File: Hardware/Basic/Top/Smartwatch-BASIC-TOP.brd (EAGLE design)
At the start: 38 x 38 mm, 60 parts, among them SW6 SWITCH.MOM, SW7 SWITCH.MOM, U2 NRF52832_MODULE_MDBT42, U4 FT231XS

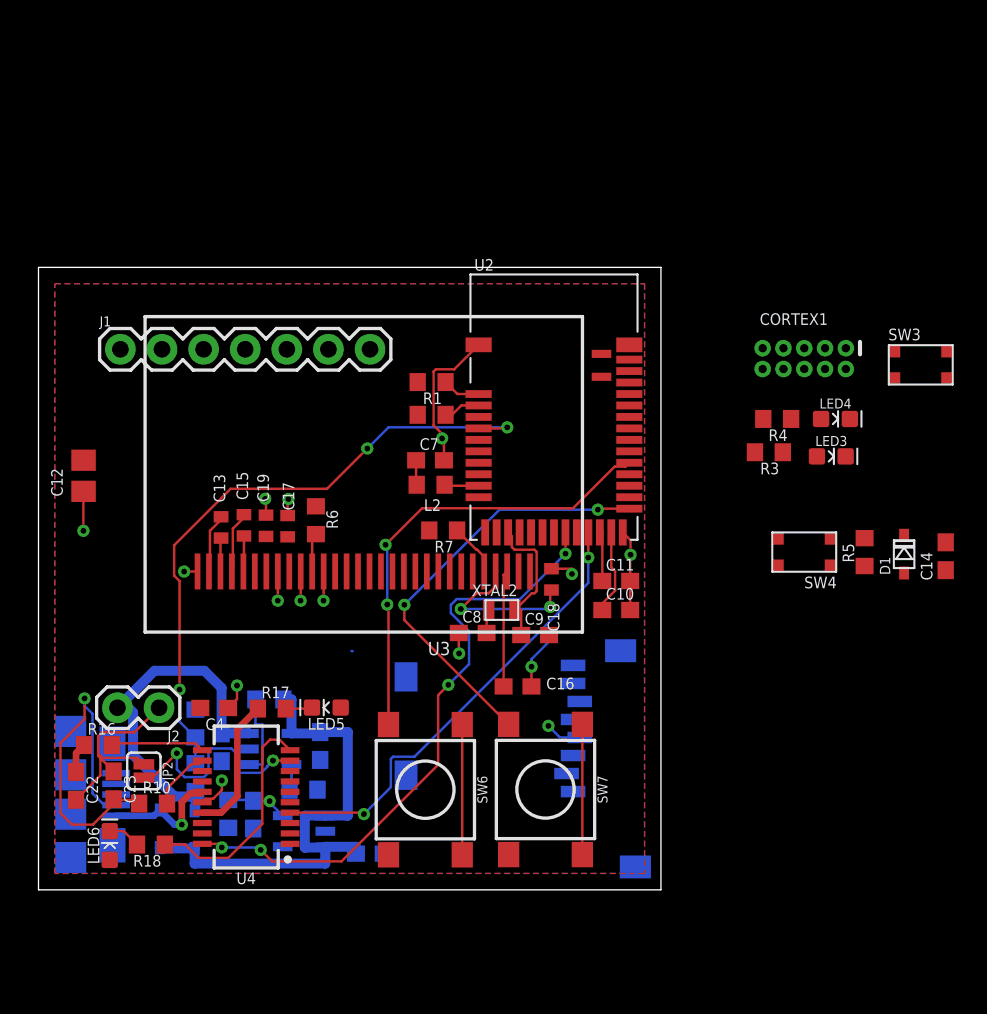
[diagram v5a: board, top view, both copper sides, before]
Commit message: Top board routing started
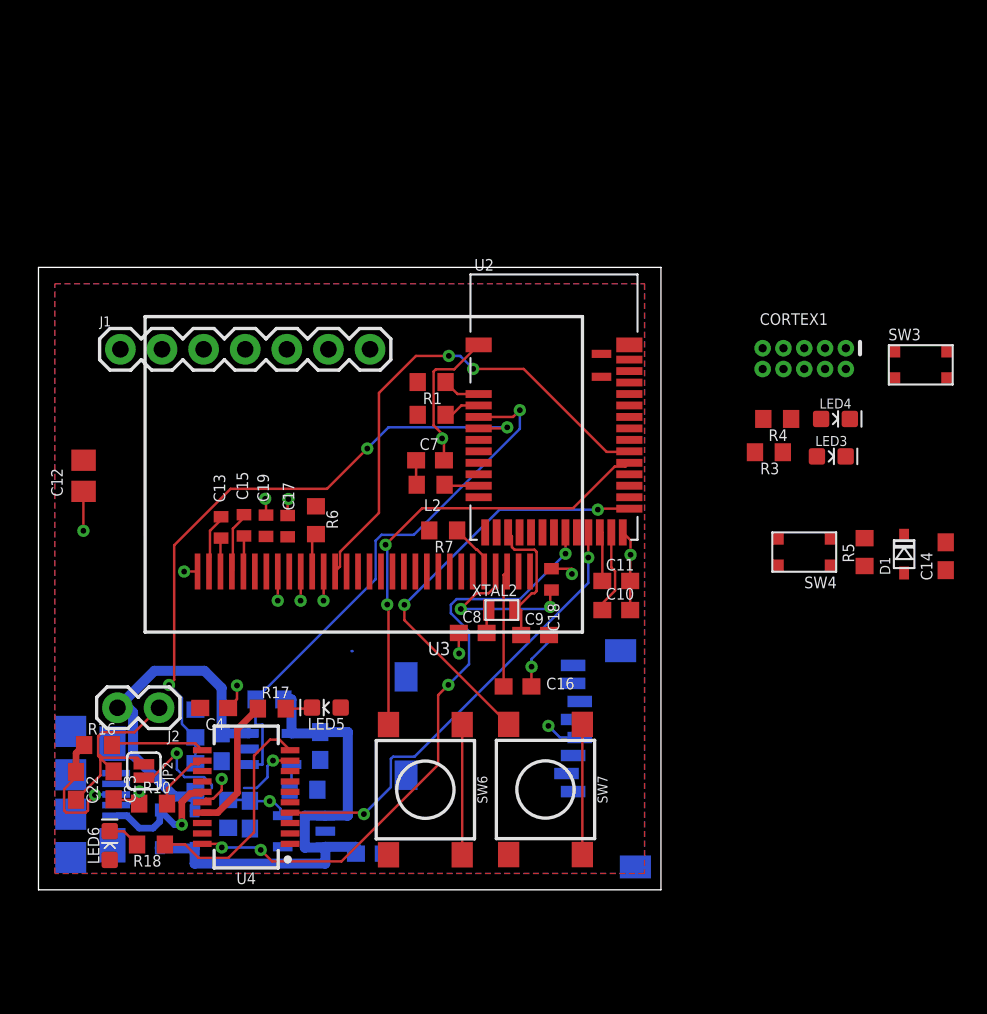
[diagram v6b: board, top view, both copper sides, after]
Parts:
- moved C6 0.20 mm to (12.9, 4.59)
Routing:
- net D16/CS.OLED: track 0.00 -> 30.7 mm, vias 0 -> 2
- net D27/CHRG.STAT: track 5.23 -> 33.4 mm, vias 0 -> 1
- net USB-: track 21.7 -> 4.58 mm
- net USB+: track 1.84 -> 8.48 mm, vias 0 -> 1
- net !CTS: track 14.4 -> 10.8 mm
- net V_USB: track 7.41 -> 8.45 mm

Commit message: Top Board Routed
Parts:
- moved LED6 1.32 mm to (3.51, 1.69), turned to 0 degrees
- moved L2 1.19 mm to (24.8, 25.5), turned to 90 degrees
- moved C7 0.94 mm to (23.3, 25.5), turned to 270 degrees
- moved C16 0.88 mm to (28.6, 13.0), turned to 90 degrees
- moved SD2 0.76 mm to (21.4, 15.4)
- moved R15 0.53 mm to (11.1, 4.62)
- moved C18 0.39 mm to (31.3, 18.6)
- moved C6 0.11 mm to (13.0, 4.60)
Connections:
- net 3.3V: now also J1.4
- net A6/TIA: now also J1.5
- net A7/PPG: now also J1.7
- net D29/LED.CTRL: now also J1.6
- net GND: now also J1.3
- net SCL: now also J1.2
- net SDA: now also J1.1
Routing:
- net SCK: track 0.00 -> 59.4 mm, vias 0 -> 2
- net 3.3V: track 6.14 -> 58.3 mm, vias 2 -> 13
- net MOSI: track 0.00 -> 42.1 mm, vias 0 -> 5
- net GND: track 48.4 -> 90.5 mm, vias 14 -> 22
- net D3/RESET.OLED: track 0.00 -> 34.8 mm, vias 0 -> 2
- net D7/SD.CS: track 0.00 -> 31.7 mm, vias 0 -> 1
- net SDA: track 2.32 -> 28.0 mm, vias 0 -> 2
- net A6/TIA: track 0.00 -> 22.0 mm, vias 0 -> 1
- net D4/DC.OLED: track 0.00 -> 21.1 mm, vias 0 -> 2
- net SCL: track 2.26 -> 22.8 mm, vias 0 -> 2
- net MISO: track 0.00 -> 19.6 mm, vias 0 -> 3
- net A7/PPG: track 0.00 -> 16.9 mm, vias 0 -> 1
- net D29/LED.CTRL: track 0.00 -> 15.1 mm, vias 0 -> 1
- net N$4: track 1.52 -> 16.5 mm, vias 0 -> 2
- net D5/CD1: track 0.00 -> 14.4 mm, vias 0 -> 1
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
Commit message: Top Board Routed
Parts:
- moved C8 0.07 mm to (26.4, 15.7)
